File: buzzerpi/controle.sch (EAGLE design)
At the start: 10 parts, among them IC1 ULN2003AN, IC2 ULN2003AN

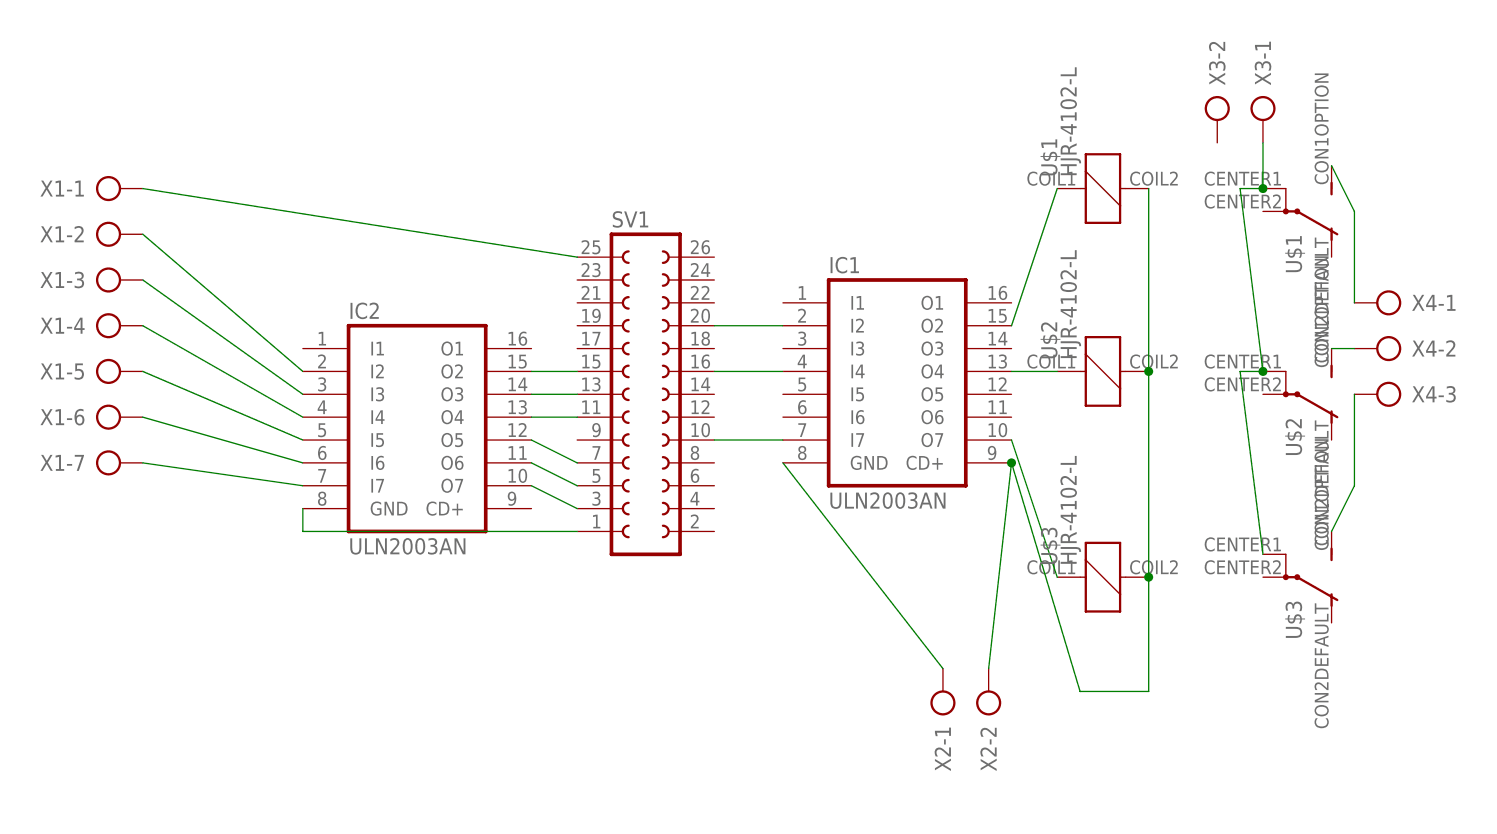
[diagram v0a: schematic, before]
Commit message: layout geändert
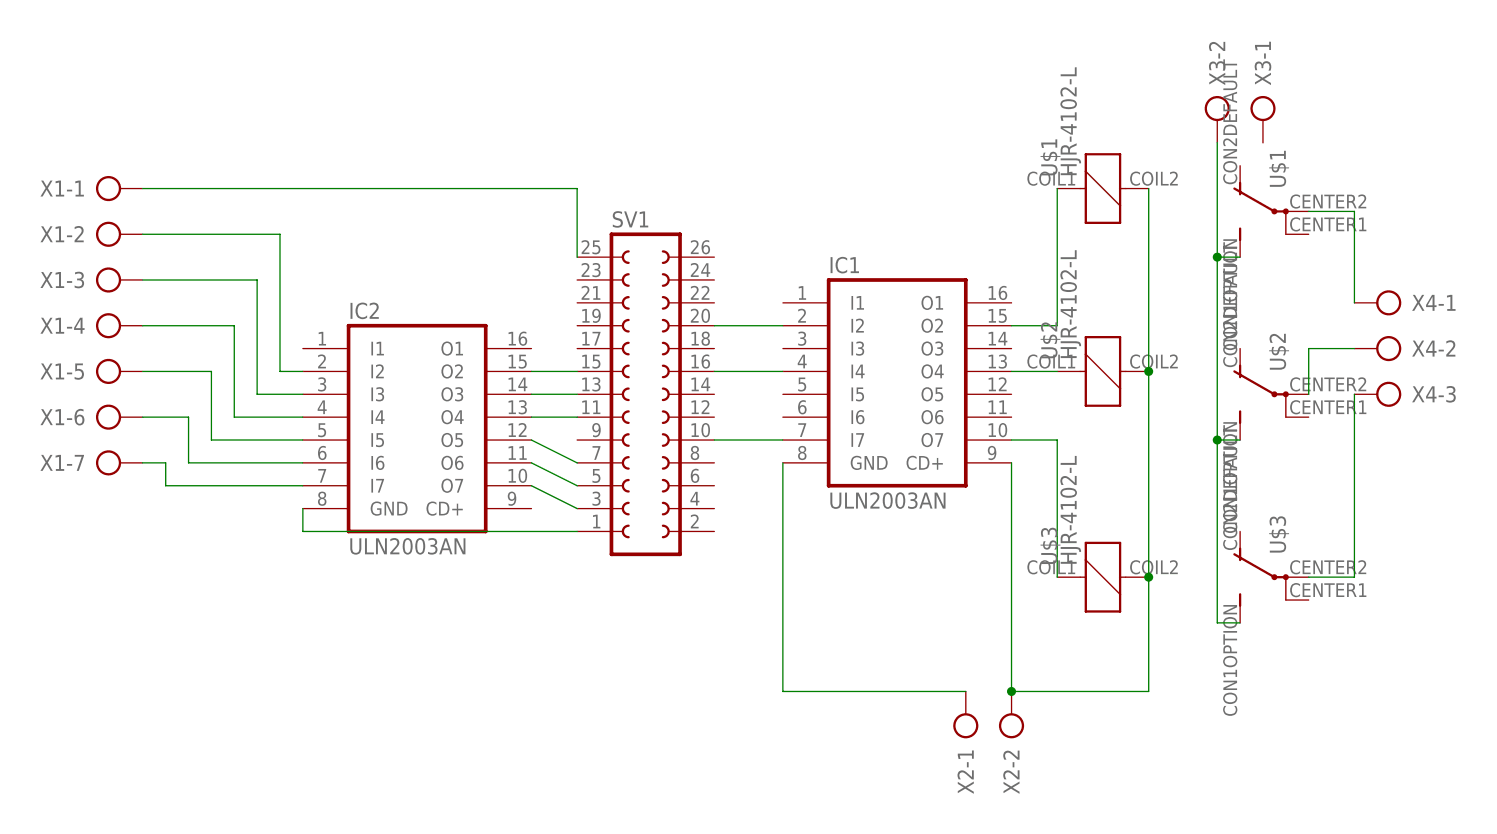
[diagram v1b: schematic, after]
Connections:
- removed net N$27: U$1G$2.P@1, U$2G$2.P@1, U$3G$2.P@1, X3-1.KL
- removed net N$28: U$2G$2.S, X4-2.KL
- removed net N$29: U$1G$2.S, X4-1.KL
- removed net N$30: U$3G$2.S, X4-3.KL
- new net N$22: U$1G$2.S, U$2G$2.S, U$3G$2.S, X3-2.KL
- new net N$23: U$1G$2.P, X4-1.KL
- new net N$25: U$2G$2.P, X4-2.KL
- new net N$26: U$3G$2.P, X4-3.KL
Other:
- moved on the sheet: U$1, U$2, U$3, X2-1, X2-2
